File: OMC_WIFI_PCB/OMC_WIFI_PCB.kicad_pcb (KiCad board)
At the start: 2 copper layers, 106.5 x 83 mm, 19 parts, among them J1 ESP32_Left, J10 Control_ACS712, J11 Control_ZMPT101B, J2 ESP32_Right, J3 Power_In, J4 Switch, J5 Pins_FT232R, J6 Line_Relay, J7 Control_Relay, J8 Line_ACS712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

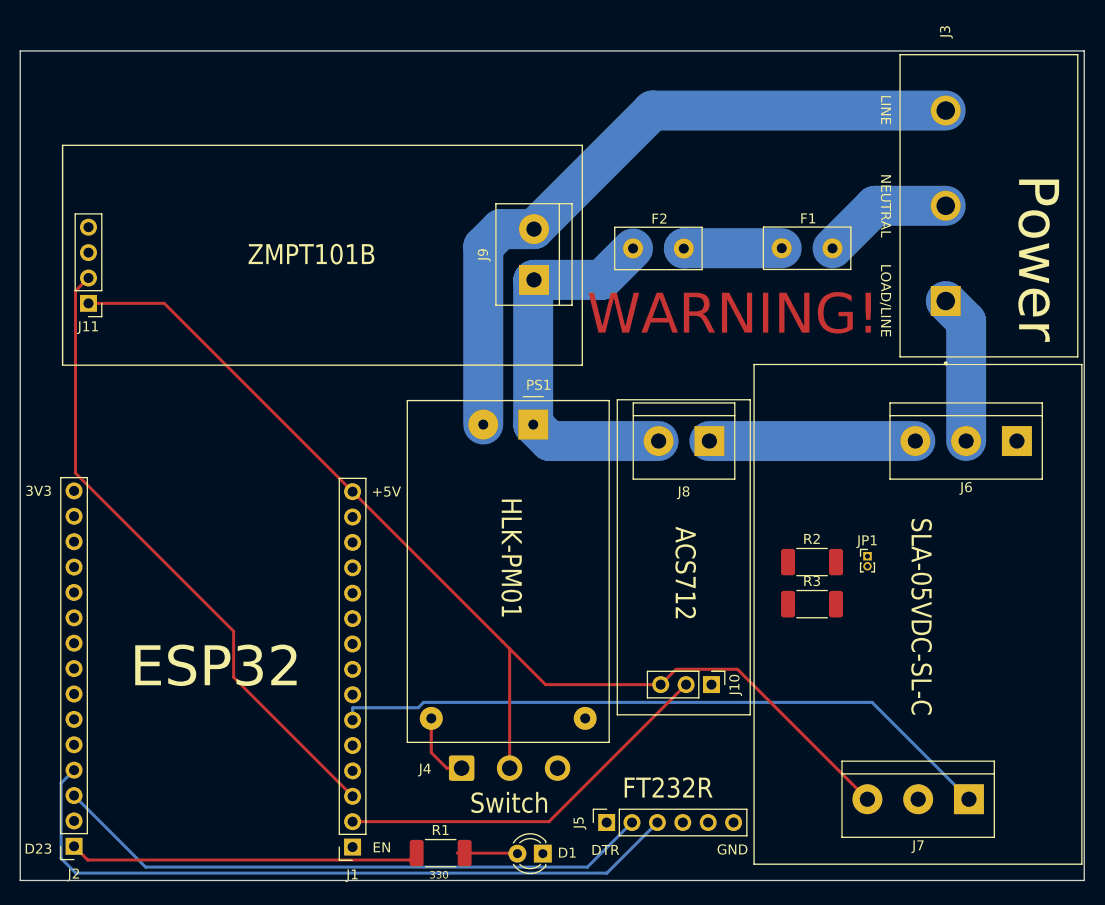
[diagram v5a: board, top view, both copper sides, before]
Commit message: Diseño PCB
+ Archivos Gerber y Drill
- Divisor de tensión del ACS712
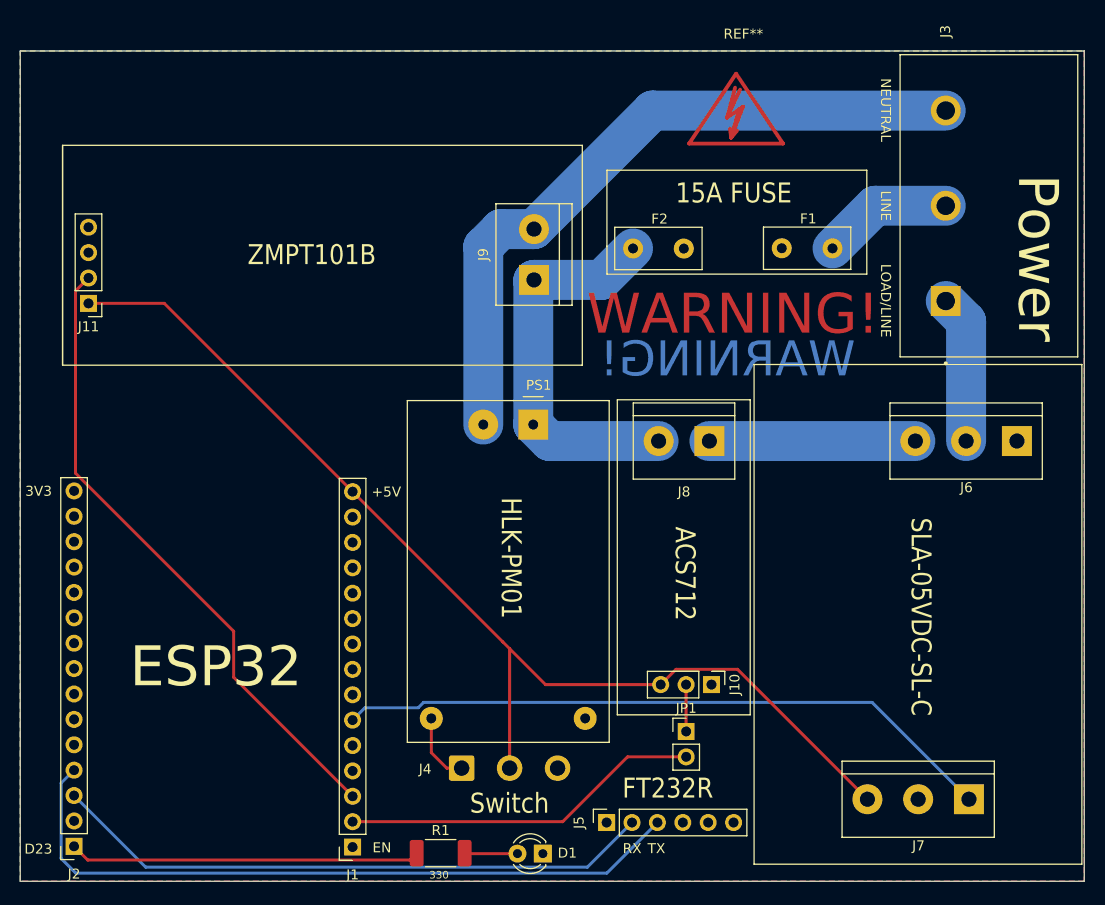
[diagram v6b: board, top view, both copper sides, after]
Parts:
- removed R2: 10K, Resistor_SMD:R_2010_5025Metric_Pad1.40x2.65mm_HandSolder
- removed R3: 20k, Resistor_SMD:R_2010_5025Metric_Pad1.40x2.65mm_HandSolder
- added REF**: Symbol_HighVoltage_Type2_CopperTop_VerySmall, Symbol:Symbol_HighVoltage_Type2_CopperTop_VerySmall, F.Cu at (644.9, -975.5)
- JP1: footprint Connector_PinHeader_1.00mm:PinHeader_1x02_P1.00mm_Vertical -> Connector_PinHeader_2.54mm:PinHeader_1x02_P2.54mm_Vertical
- moved JP1 25.2 mm to (639.9, -913.8)
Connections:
- F2 pad 2: Net-(F1-Pad1) -> Net-(F2-Pad2)
- JP1 pad 2: Net-(JP1-Pad2) -> VP_ACS
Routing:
- net Net-(F1-Pad1): track 9.81 -> 0.00 mm
- net Net-(J10-Pad2): track 0.00 -> 4.69 mm
- net VP_ACS: track 39.1 -> 36.1 mm
- net D32_RELAY: track 67.1 -> 66.4 mm
- added copper zone on B.Cu, net GND
- added copper zone on F.Cu, net GND
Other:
- board size 106.5 x 83 mm -> 106.5 x 83.1 mm
- board text added: "15A FUSE"
- board text added: "RX"
- board text added: "TX"
- board text removed: "DTR"
- board text removed: "GND"

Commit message: Diseño PCB
> Modificación de dimensiones ESP32 Devkit V1 en PCB.
> Modificadas las dimensiones de la placa.
+ Pistas entre puntas de fusible para aumentar área de contacto con soldadura.
> Generados nuevos archivos gerber
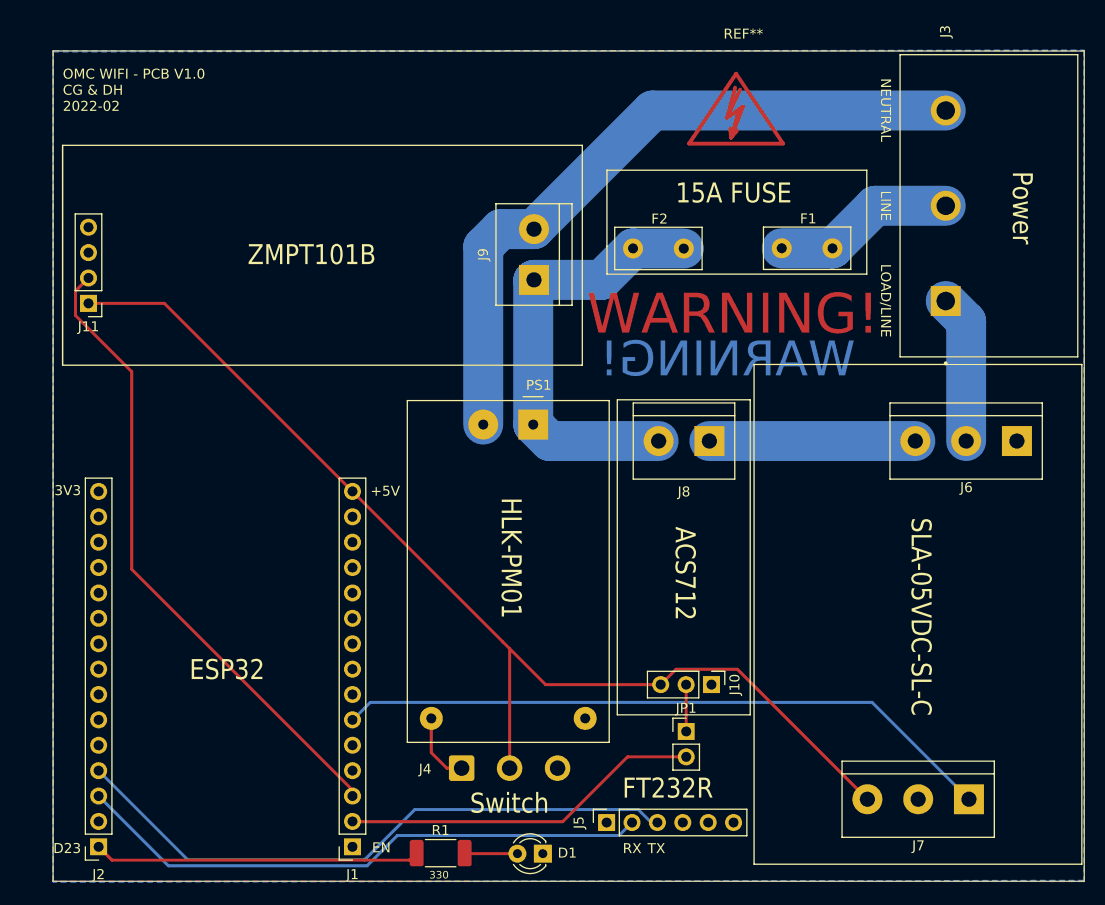
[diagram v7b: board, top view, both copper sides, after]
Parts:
- moved J2 2.46 mm to (581.1, -902.3)
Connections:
- F1 pad 2: Net-(F1-Pad2) -> Net-(F1-Pad1)
- F2 pad 2: Net-(F2-Pad2) -> LINE
- J3 pad 2: Net-(F1-Pad2) -> Net-(F1-Pad1)
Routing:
- net Net-(F1-Pad1): track 0.00 -> 18.2 mm
- net Net-(F1-Pad2): track 13.1 -> 0.00 mm
- net RX0: track 71.7 -> 62.2 mm
- net LINE: track 38.9 -> 44.0 mm
- net TX0: track 60.6 -> 58.1 mm
- net D23_LED: track 35.1 -> 33.6 mm
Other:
- board size 106.5 x 83.1 mm -> 103.2 x 83.1 mm
- board text added: "OMC WIFI - PCB V1.0 CG & DH 2022-02"

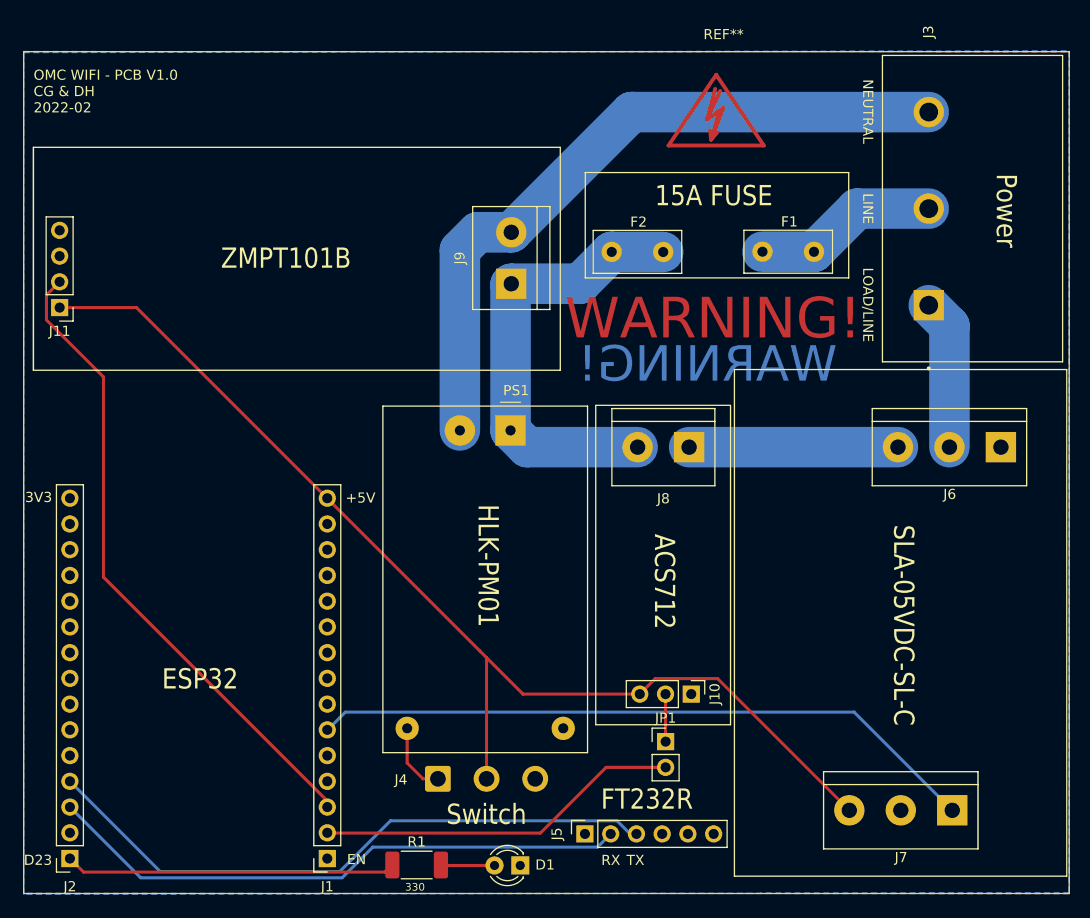
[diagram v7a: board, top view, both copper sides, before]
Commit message: Modificación PCB
> Redimensionamiento Relay
> Redimensionamiento ACS
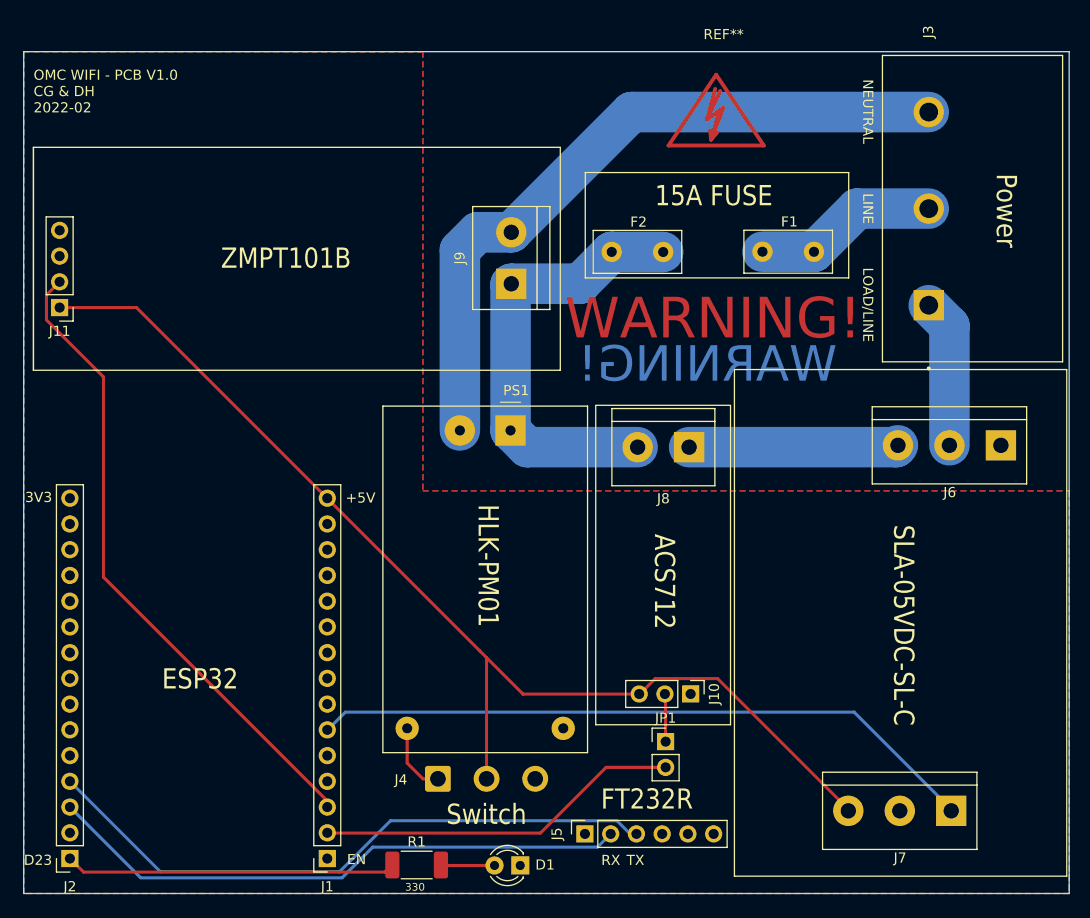
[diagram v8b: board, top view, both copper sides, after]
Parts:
- moved J6 0.18 mm to (673.0, -943.1)
- moved J7 0.11 mm to (668.1, -907.0)
- moved J10 0.06 mm to (642.4, -918.5)
